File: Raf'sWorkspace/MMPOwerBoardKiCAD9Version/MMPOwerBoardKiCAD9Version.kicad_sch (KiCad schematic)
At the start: 103 parts, among them J1 TYPE-C-31-M-04, J2 Conn_02x16_Odd_Even, J3 Conn_01x02, Q1 SS8050, SW1 SS-12D11-G050, U1 HUSB237, U10 TPS22917DBVR, U11 AMS1117-5.0, U2 TP4056-42-ESOP8, U3 DRV8833PWPR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

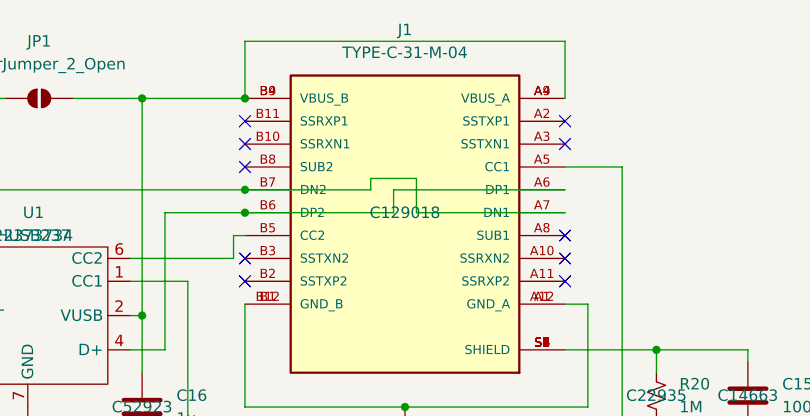
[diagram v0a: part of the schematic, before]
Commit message: Changed the USB-C connector, and connected it - removed Ground layers, changed silkscreens for a few units
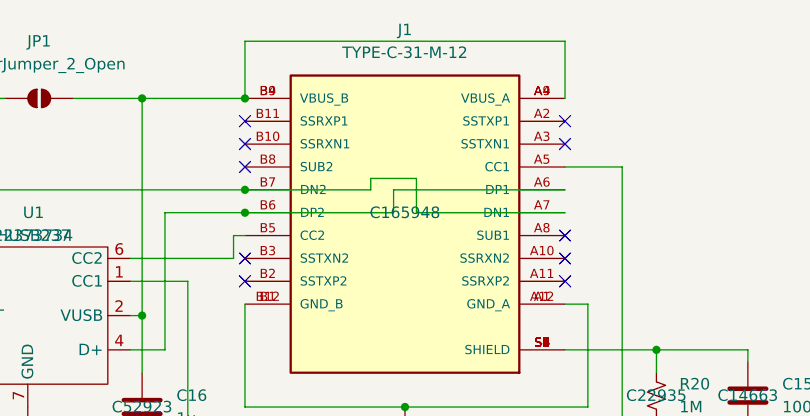
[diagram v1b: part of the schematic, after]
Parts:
- J1: value TYPE-C-31-M-04 -> TYPE-C-31-M-12; footprint TYPE-C-31-M-04:HRO_TYPE-C-31-M-04 -> TYPE-C-31-M-04:USB-C_SMD-TYPE-C-31-M-12; LCSC C129018 -> C165948
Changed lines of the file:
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@@
 			)
 		)
-		(property "Value" "TYPE-C-31-M-04"
+		(property "Value" "TYPE-C-31-M-12"
 			(at 360.68 17.78 0)
 			(effects
@@
 			)
 		)
-		(property "Footprint" "TYPE-C-31-M-04:HRO_TYPE-C-31-M-04"
+		(property "Footprint" "TYPE-C-31-M-04:USB-C_SMD-TYPE-C-31-M-12"
 			(at 360.68 35.56 0)
 			(effects
@@
 			)
 		)
-		(property "LCSC" "C129018"
+		(property "LCSC" "C165948"
 			(at 360.68 35.56 0)
 			(effects

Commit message: Added the JLC PCB submission pcis and stuff [named incorrectedly
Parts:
- U3, U9: footprint DRV8833PWPR:IC_DRV8833PWPR -> Package_SO:HTSSOP-16-1EP_4.4x5mm_P0.65mm_EP3.4x5mm
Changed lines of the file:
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@@
 			)
 		)
-		(property "Footprint" "DRV8833PWPR:IC_DRV8833PWPR"
+		(property "Footprint" "Package_SO:HTSSOP-16-1EP_4.4x5mm_P0.65mm_EP3.4x5mm"
 			(at 196.85 179.07 0)
 			(effects
@@
 			)
 		)
-		(property "Footprint" "DRV8833PWPR:IC_DRV8833PWPR"
+		(property "Footprint" "Package_SO:HTSSOP-16-1EP_4.4x5mm_P0.65mm_EP3.4x5mm"
 			(at 270.51 179.07 0)
 			(effects
